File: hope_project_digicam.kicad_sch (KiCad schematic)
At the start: 22 parts, among them J1 TFT_Pin_Socket, J1 USB_C_Receptacle_USB2.0_16P, J2 SD_Card_Port, J3 Camera_Pin_Out, J4 Lipo battery input, Q1 NMOS, SW1 SW_Push, SW2 Reset, SW3 Boot, U1 ESP32-S3-WROOM-1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

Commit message: finished schematic
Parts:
- removed C1: 1uF, symbol Device:C
- removed U2: AP7332-3333W6-7, SOT26_DIO, symbol 2026-03-12_05-38-18:AP7332-3333W6-7
- added C5: 0.1uF, symbol Device:C
- added C6: 22uF, symbol Device:C
- added D2: D_Schottky, symbol Device:D_Schottky
- added Q2: PMOS, symbol Simulation_SPICE:PMOS
- added R10, R11, R7, R8, R9: 10k, symbol Device:R
- added R12: 100k, symbol Device:R
- added U3: AP2112K-3.3, Package_TO_SOT_SMD:SOT-23-5, symbol Regulator_Linear:AP2112K-3.3
- J4: value Lipo battery input -> Lipo batt in
- R5: value R -> 10
- R6: value R -> 10k
- renumbered J1 to J5
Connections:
- net +3.3V: now also J2.4 (VDD), J3.1 (Pin_1), J5.1 (Pin_1), R5.2, C5.1, C6.1, R10.1, R11.1, R7.1, R8.1, R9.1, U3.5 (VOUT); no longer C2.1
- net GND: now also J2.3 (VSS), J2.6 (VSS__1), J2.G1 (GND), J2.G2 (GND__1), J3.2 (Pin_2), J5.3 (Pin_3), SW1.2, C5.2, C6.2, R12.1, U3.2 (GND)
- net TFT_SDCS: now reaches J5.10 (Pin_10)
- net TFT_LIT: now reaches J5.11 (Pin_11)
- net TFT_LIT: now also U1.25 (IO48)
- net 3.3V_OUT: now reaches J5.2 (Pin_2)
- net TFT_SCK: now reaches J5.4 (Pin_4)
- net TFT_SCK: now also U1.31 (IO38)
- net TFT_MISO: now reaches J5.5 (Pin_5)
- net TFT_MOSI: now reaches J5.6 (Pin_6)
- net TFT_MOSI: now also U1.32 (IO39)
- net TFT_CS: now reaches J5.7 (Pin_7)
- net TFT_CS: now also U1.17 (IO9)
- net TFT_RST: now reaches J5.8 (Pin_8)
- net TFT_RST: now also C4.2, R1.2, SW2.2, U1.3 (EN)
- net TFT_DC: now reaches J5.9 (Pin_9)
- net TFT_DC: now also U1.16 (IO46)
- net SD_CS: now reaches J2.1 (DAT3/CD)
- net SD_CS: now also U1.18 (IO10), R9.2
- net SD_MOSI: now reaches J2.2 (CMD)
- net SD_MOSI: now also U1.19 (IO11), R7.2
- net SD_SCK: now reaches J2.5 (CLK)
- net SD_SCK: now also U1.20 (IO12)
- net SD_MISO: now reaches J2.7 (DAT0)
- net SD_MISO: now also U1.21 (IO13), R8.2
- net SD_DAT1: now reaches J2.8 (DAT1)
- net SD_DAT1: now also R10.2
- net SD_DAT2: now reaches J2.9 (DAT2)
- net SD_DAT2: now also R11.2
- net CAM_D8: now reaches J3.10 (Pin_10)
- net CAM_D8: now also U1.10 (IO17)
- net CAM_D7: now reaches J3.11 (Pin_11)
- net CAM_D7: now also U1.9 (IO16)
- net CAM_D6: now reaches J3.12 (Pin_12)
- net CAM_D6: now also U1.8 (IO15)
- net CAM_D5: now reaches J3.13 (Pin_13)
- net CAM_D5: now also U1.7 (IO7)
- net CAM_D4: now reaches J3.14 (Pin_14)
- net CAM_D4: now also U1.6 (IO6)
- net CAM_D3: now reaches J3.15 (Pin_15)
- net CAM_D3: now also U1.5 (IO5)
- net CAM_D2: now reaches J3.16 (Pin_16)
- net CAM_D2: now also U1.4 (IO4)
- net CAM_RT: now reaches J3.17 (Pin_17)
- net CAM_PD: now reaches J3.18 (Pin_18)
- net CAM_SCL: now reaches J3.3 (Pin_3)
- net CAM_SCL: now also U1.39 (IO1)
- net CAM_SDA: now reaches J3.4 (Pin_4)
- net CAM_SDA: now also U1.38 (IO2)
- net CAM_VS: now reaches J3.5 (Pin_5)
- net CAM_VS: now also U1.24 (IO47)
- net CAM_HS: now reaches J3.6 (Pin_6)
- net CAM_HS: now also U1.23 (IO21)
- net CAM_PC: now reaches J3.7 (Pin_7)
- net CAM_PC: now also U1.12 (IO8)
- net CAM_XC: now reaches J3.8 (Pin_8)
- net CAM_XC: now also U1.15 (IO3)
- net CAM_D9: now reaches J3.9 (Pin_9)
- net CAM_D9: now also U1.11 (IO18)
- net CAM_TRIGGER: now reaches SW1.1
- net CAM_TRIGGER: now also U1.22 (IO14)
- net LED: now reaches R4.1
- net LED: now also U1.26 (IO45)
- net VCC renamed VBUS
- net VBUS: now also D2.2 (A), Q2.2 (G), R12.2; no longer J4.2 (Pin_2), R5.2
- new net +BATT: J4.2 (Pin_2), Q2.1 (D)
- new net PWR_IN: C2.1, D2.1 (K), Q2.3 (S), U3.1 (VIN), U3.3 (EN)
- no-connect marks 2 -> 17
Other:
- note added: "Camera Button Trigger"
- note added: "Camera Pins"
- note added: "ESP32-S3-WROOM-1"
- note added: "Flash / LED"
- note added: "Lipo power in + LDO to 3.3V"
- note added: "SD Card Port"
- note added: "TFT Screen Pins"
- note added: "TFT_MISO is 3.3V because write-only, can leave unconnected"
- note added: "USB-C Power and Data"
- moved on the sheet: C3, C4, D1, J1, J2, J3, J4, J5, Q1, R1, R2, R3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

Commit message: added test points
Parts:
- added J6: extra, symbol Connector:Conn_01x02_Socket
- added TP1, TP10, TP11, TP12, TP13, TP2, TP3, TP4, TP5, TP6, TP7, TP8, TP9: TestPoint, symbol Connector:TestPoint
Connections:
- net +3.3V: now also TP1.1
- net +BATT: now also TP2.1
- net CAM_PC: now also TP9.1
- net CAM_SCL: now also TP7.1
- net CAM_SDA: now also TP8.1
- net GND: now also TP5.1, TP6.1
- net PWR_IN: now also TP3.1
- net SD_MISO: now also TP12.1
- net SD_MOSI: now also TP11.1
- net SD_SCK: now also TP10.1
- net VBUS: now also TP4.1
- net at Q1.2 (G), R4.2, R6.1: now also TP13.1
- net at U1.36 (RXD0): now also J6.2 (Pin_2)
- net at U1.37 (TXD0): now also J6.1 (Pin_1)
- no-connect marks 17 -> 15
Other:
- moved on the sheet: D1, J3, J5, Q1, R4, R5, R6, SW1

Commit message: layout progress
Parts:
- C2, C3, C4: footprint (none) -> HOPE DigiCam:1uF_Cap
- C5: footprint (none) -> HOPE DigiCam:0.1u_Cap
- C6: footprint (none) -> HOPE DigiCam:22u_Cap
- D1: footprint (none) -> LED_SMD:LED_1206_3216Metric
- D2: footprint (none) -> HOPE DigiCam:Shottky_Diode
- J1: footprint (none) -> HOPE DigiCam:USB_C_Receptacle
- J2: footprint 10067847-001RLF:AMPHENOL_10067847-001RLF -> HOPE DigiCam:SD_Card_Conn
- J3, J5, J6: footprint (none) -> HOPE DigiCam:40_Pin_Conn
- J4: footprint (none) -> HOPE DigiCam:Right_Angle_Conn
- Q1: footprint (none) -> HOPE DigiCam:NMOS
- Q2: footprint (none) -> HOPE DigiCam:PMOS
- R1, R5: footprint (none) -> HOPE DigiCam:10_Res
- R10, R11, R6, R7, R8, R9: footprint (none) -> HOPE DigiCam:10k_Res
- R12: footprint (none) -> HOPE DigiCam:100k_Res
- R2, R3: footprint (none) -> HOPE DigiCam:5.1k_Res
- R4: footprint (none) -> HOPE DigiCam:100_Res
- SW2, SW3: footprint (none) -> HOPE DigiCam:SW2_SW3
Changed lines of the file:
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@@
 			)
 		)
-		(property "Footprint" ""
+		(property "Footprint" "HOPE DigiCam:Right_Angle_Conn"
 			(at 26.67 34.29 0)
 			(effects
@@
 			)
 		)
-		(property "Footprint" ""
+		(property "Footprint" "HOPE DigiCam:40_Pin_Conn"
 			(at 234.95 100.33 0)
 			(effects
@@
 			)
 		)
-		(property "Footprint" ""
+		(property "Footprint" "HOPE DigiCam:5.1k_Res"
 			(at 62.738 80.01 90)
 			(effects
@@
 			)
 		)
-		(property "Footprint" "10067847-001RLF:AMPHENOL_10067847-001RLF"
+		(property "Footprint" "HOPE DigiCam:SD_Card_Conn"
 			(at 83.82 153.67 0)
 			(effects
@@
 			)
 		)
-		(property "Footprint" ""
+		(property "Footprint" "HOPE DigiCam:PMOS"
 			(at 80.01 27.94 0)
 			(effects
@@
 			)
 		)
-		(property "Footprint" ""
+		(property "Footprint" "HOPE DigiCam:10_Res"
 			(at 106.172 63.5 90)
 			(effects
@@
 			)
 		)
-		(property "Footprint" ""
+		(property "Footprint" "HOPE DigiCam:22u_Cap"
 			(at 187.6552 69.85 0)
 			(effects
@@
 			)
 		)
-		(property "Footprint" ""
+		(property "Footprint" "HOPE DigiCam:SW2_SW3"
 			(at 96.52 83.82 0)
 			(effects
@@
 			)
 		)
-		(property "Footprint" ""
+		(property "Footprint" "HOPE DigiCam:40_Pin_Conn"
 			(at 165.1 67.31 0)
 			(effects
@@
 			)
 		)
-		(property "Footprint" ""
+		(property "Footprint" "HOPE DigiCam:SW2_SW3"
 			(at 99.06 62.23 0)
 			(effects
@@
 			)
 		)
-		(property "Footprint" ""
+		(property "Footprint" "HOPE DigiCam:NMOS"
 			(at 163.83 172.72 0)
 			(effects
@@
 			)
 		)
-		(property "Footprint" ""
+		(property "Footprint" "HOPE DigiCam:1uF_Cap"
 			(at 103.8352 36.83 0)
 			(effects
@@
 			)
 		)
-		(property "Footprint" ""
+		(property "Footprint" "HOPE DigiCam:40_Pin_Conn"
 			(at 224.79 148.59 0)
 			(effects
@@
 			)
 		)
-		(property "Footprint" ""
+		(property "Footprint" "HOPE DigiCam:5.1k_Res"
 			(at 70.358 77.47 90)
 			(effects
@@
 			)
 		)
-		(property "Footprint" ""
+		(property "Footprint" "HOPE DigiCam:10k_Res"
 			(at 40.132 179.07 90)
 			(effects
@@
 			)
 		)
-		(property "Footprint" ""
+		(property "Footprint" "HOPE DigiCam:10k_Res"
 			(at 27.432 179.07 90)
 			(effects
@@
 			)
 		)
-		(property "Footprint" ""
+		(property "Footprint" "HOPE DigiCam:10k_Res"
 			(at 54.102 149.86 90)
 			(effects
@@
 			)
 		)
-		(property "Footprint" ""
+		(property "Footprint" "HOPE DigiCam:10_Res"
 			(at 163.068 154.94 90)
 			(effects
@@
 			)
 		)
-		(property "Footprint" ""
+		(property "Footprint" "HOPE DigiCam:100k_Res"
 			(at 67.818 34.29 90)
 			(effects
@@
 			)
 		)
-		(property "Footprint" ""
+		(property "Footprint" "HOPE DigiCam:0.1u_Cap"
 			(at 173.6852 69.85 0)
 			(effects
@@
 			)
 		)
-		(property "Footprint" ""
+		(property "Footprint" "LED_SMD:LED_1206_3216Metric"
 			(at 161.29 163.83 0)
 			(effects
@@
 			)
 		)
-		(property "Footprint" ""
+		(property "Footprint" "HOPE DigiCam:1uF_Cap"
 			(at 102.87 73.9648 0)
 			(effects
@@
 			)
 		)
-		(property "Footprint" ""
+		(property "Footprint" "HOPE DigiCam:10k_Res"
 			(at 24.892 160.02 90)
 			(effects
@@
 			)
 		)
-		(property "Footprint" ""
+		(property "Footprint" "HOPE DigiCam:10k_Res"
 			(at 37.592 152.4 90)
 			(effects
@@
 			)
 		)
-		(property "Footprint" ""
+		(property "Footprint" "HOPE DigiCam:100_Res"
 			(at 147.32 177.038 90)
 			(effects
@@
 			)
 		)
-		(property "Footprint" ""
+		(property "Footprint" "HOPE DigiCam:10k_Res"
 			(at 154.94 185.928 90)
 			(effects
@@
 			)
 		)
-		(property "Footprint" ""
+		(property "Footprint" "HOPE DigiCam:USB_C_Receptacle"
 			(at 39.37 83.82 0)
 			(effects
@@
 			)
 		)
-		(property "Footprint" ""
+		(property "Footprint" "HOPE DigiCam:Shottky_Diode"
 			(at 57.15 63.5 0)
 			(effects
@@
 			)
 		)
-		(property "Footprint" ""
+		(property "Footprint" "HOPE DigiCam:1uF_Cap"
 			(at 136.8552 36.83 0)
 			(effects

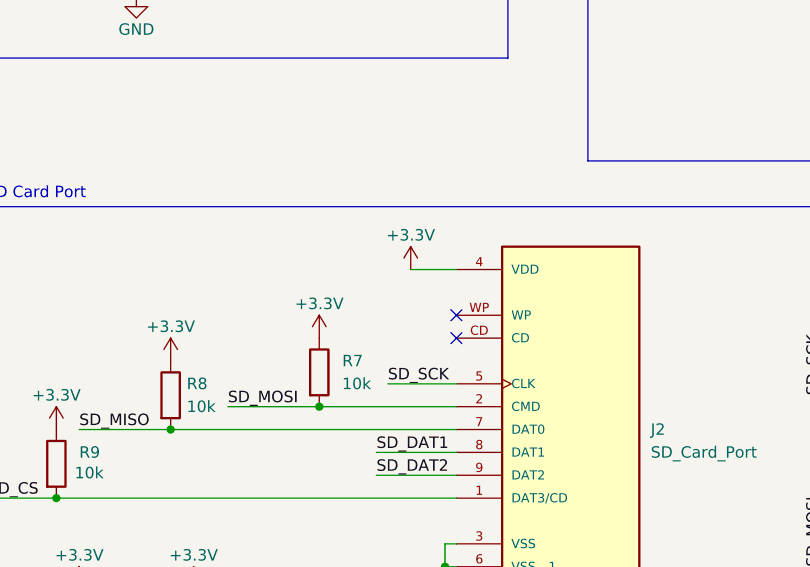
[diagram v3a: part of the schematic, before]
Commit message: fixed footprints
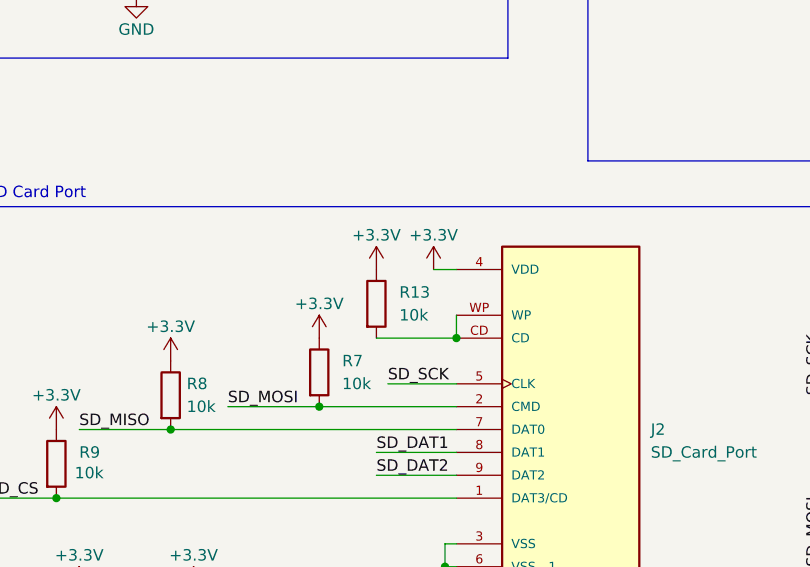
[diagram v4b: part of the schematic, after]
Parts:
- added R13: 10k, HOPE DigiCam:10k_Res, symbol Device:R
- J3: footprint HOPE DigiCam:40_Pin_Conn -> Connector_PinSocket_2.54mm:PinSocket_2x09_P2.54mm_Vertical
- J5: footprint HOPE DigiCam:40_Pin_Conn -> Connector_PinSocket_2.54mm:PinSocket_1x11_P2.54mm_Vertical
- SW1: footprint (none) -> HOPE DigiCam:SW2_SW3
- TP1, TP10, TP11, TP12, TP13, TP2, TP3, TP4, TP5, TP6, TP7, TP8, TP9: footprint (none) -> TestPoint:TestPoint_Plated_Hole_D2.0mm
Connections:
- net +3.3V: now also R13.1
- net at J2.CD: now also J2.WP, R13.2
- no-connect marks 15 -> 13
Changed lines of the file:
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@@
 	)
 	(junction
+		(at 71.12 146.05)
+		(diameter 0)
+		(color 0 0 0 0)
+	)
+	(junction
 		(at 39.37 156.21)
 		(diameter 0)
@@
 	)
 	(no_connect
-		(at 71.12 146.05)
-	)
-	(no_connect
-		(at 71.12 143.51)
-	)
-	(no_connect
 		(at 50.8 96.52)
 	)
@@
 	(wire
 		(pts
+			(xy 62.23 146.05) (xy 71.12 146.05)
+		)
+		(stroke
+			(width 0)
+			(type default)
+		)
+	)
+	(wire
+		(pts
 			(xy 219.71 105.41) (xy 229.87 105.41)
 		)
@@
 	(wire
 		(pts
+			(xy 68.58 138.43) (xy 71.12 138.43)
+		)
+		(stroke
+			(width 0)
+			(type default)
+		)
+	)
+	(wire
+		(pts
 			(xy 154.94 92.71) (xy 165.1 92.71)
 		)
@@
 	(wire
 		(pts
+			(xy 71.12 143.51) (xy 71.12 146.05)
+		)
+		(stroke
+			(width 0)
+			(type default)
+		)
+	)
+	(wire
+		(pts
 			(xy 209.55 153.67) (xy 219.71 153.67)
 		)
@@
 	(wire
 		(pts
-			(xy 66.04 138.43) (xy 71.12 138.43)
-		)
-		(stroke
-			(width 0)
-			(type default)
-		)
-	)
-	(wire
-		(pts
 			(xy 105.41 67.31) (xy 105.41 74.93)
 		)
@@
 			)
 		)
-		(property "Footprint" ""
+		(property "Footprint" "TestPoint:TestPoint_Plated_Hole_D2.0mm"
 			(at 116.84 180.34 0)
 			(effects
@@
 			)
 		)
-		(property "Footprint" "HOPE DigiCam:40_Pin_Conn"
+		(property "Footprint" "Connector_PinSocket_2.54mm:PinSocket_1x11_P2.54mm_Vertical"
 			(at 234.95 100.33 0)
 			(effects
@@
 			)
 		)
-		(property "Footprint" ""
+		(property "Footprint" "TestPoint:TestPoint_Plated_Hole_D2.0mm"
 			(at 163.83 35.56 0)
 			(effects
@@
 			)
 		)
-		(property "Footprint" ""
+		(property "Footprint" "TestPoint:TestPoint_Plated_Hole_D2.0mm"
 			(at 156.21 171.45 0)
 			(effects
@@
 			)
 		)
-		(property "Footprint" ""
+		(property "Footprint" "TestPoint:TestPoint_Plated_Hole_D2.0mm"
 			(at 116.84 142.24 0)
 			(effects
@@
 			)
 		)
-		(property "Footprint" ""
+		(property "Footprint" "TestPoint:TestPoint_Plated_Hole_D2.0mm"
 			(at 166.37 26.67 0)
 			(effects
@@
 			)
 		)
-		(property "Footprint" "HOPE DigiCam:40_Pin_Conn"
+		(property "Footprint" "Connector_PinSocket_2.54mm:PinSocket_2x09_P2.54mm_Vertical"
 			(at 224.79 148.59 0)
 			(effects
@@
 			)
 		)
-		(property "Footprint" ""
+		(property "Footprint" "TestPoint:TestPoint_Plated_Hole_D2.0mm"
 			(at 181.61 35.56 0)
 			(effects
@@
 			)
 		)
-		(property "Footprint" ""
+		(property "Footprint" "TestPoint:TestPoint_Plated_Hole_D2.0mm"
 			(at 274.32 144.78 0)
 			(effects
@@
 	(symbol
 		(lib_id "power:+3.3V")
-		(at 66.04 138.43 0)
+		(at 62.23 138.43 0)
+		(unit 1)
+		(exclude_from_sim no)
+		(in_bom yes)
+		(on_board yes)
+		(dnp no)
+		(property "Reference" "#PWR039"
+			(at 62.23 142.24 0)
+			(effects
+				(font
+					(size 1.27 1.27)
+				)
+				(hide yes)
+			)
+		)
+		(property "Value" "+3.3V"
+			(at 62.23 134.62 0)
+			(effects
+				(font
+					(size 1.27 1.27)
+				)
+			)
+		)
+		(property "Footprint" ""
+			(at 62.23 138.43 0)
+			(effects
+				(font
+					(size 1.27 1.27)
+				)
+				(hide yes)
+			)
+		)
+		(property "Datasheet" ""
+			(at 62.23 138.43 0)
+			(effects
+				(font
+					(size 1.27 1.27)
+				)
+				(hide yes)
+			)
+		)
+		(property "Description" "Power symbol creates a global label with name \"+3.3V\""
+			(at 62.23 138.43 0)
+			(effects
+				(font
+					(size 1.27 1.27)
+				)
+				(hide yes)
+			)
+		)
+		(pin "1"
+		)
+		(instances
+			(project "hope_project_digicam"
+				(path "/cbe9fd98-ee86-44ac-bda3-802b626f1144"
+					(reference "#PWR039")
+					(unit 1)
+				)
+			)
+		)
+	)
+	(symbol
+		(lib_id "power:+3.3V")
+		(at 68.58 138.43 0)
 		(unit 1)
 		(exclude_from_sim no)
@@
 		(dnp no)
 		(property "Reference" "#PWR024"
-			(at 66.04 142.24 0)
+			(at 68.58 142.24 0)
 			(effects
 				(font
@@
 		)
 		(property "Value" "+3.3V"
-			(at 66.04 134.62 0)
+			(at 68.58 134.62 0)
 			(effects
 				(font
@@
 		)
 		(property "Footprint" ""
-			(at 66.04 138.43 0)
+			(at 68.58 138.43 0)
 			(effects
 				(font
@@
 		)
 		(property "Datasheet" ""
-			(at 66.04 138.43 0)
+			(at 68.58 138.43 0)
 			(effects
 				(font
@@
 		)
 		(property "Description" "Power symbol creates a global label with name \"+3.3V\""
-			(at 66.04 138.43 0)
+			(at 68.58 138.43 0)
 			(effects
 				(font
@@
 			)
 		)
-		(property "Footprint" ""
+		(property "Footprint" "HOPE DigiCam:SW2_SW3"
 			(at 226.06 60.96 0)
 			(effects
@@
 			)
 		)
-		(property "Footprint" ""
+		(property "Footprint" "TestPoint:TestPoint_Plated_Hole_D2.0mm"
 			(at 116.84 161.29 0)
 			(effects
@@
 			)
 		)
-		(property "Footprint" ""
+		(property "Footprint" "TestPoint:TestPoint_Plated_Hole_D2.0mm"
 			(at 257.81 135.89 0)
 			(effects
@@
 			)
 		)
-		(property "Footprint" ""
+		(property "Footprint" "TestPoint:TestPoint_Plated_Hole_D2.0mm"
 			(at 257.81 153.67 0)
 			(effects
@@
 	)
 	(symbol
+		(lib_id "Device:R")
+		(at 62.23 142.24 0)
+		(unit 1)
+		(exclude_from_sim no)
+		(in_bom yes)
+		(on_board yes)
+		(dnp no)
+		(property "Reference" "R13"
+			(at 64.77 140.9699 0)
+			(effects
+				(font
+					(size 1.27 1.27)
+				)
+				(justify left)
+			)
+		)
+		(property "Value" "10k"
+			(at 64.77 143.5099 0)
+			(effects
+				(font
+					(size 1.27 1.27)
+				)
+				(justify left)
+			)
+		)
+		(property "Footprint" "HOPE DigiCam:10k_Res"
+			(at 60.452 142.24 90)
+			(effects
+				(font
+					(size 1.27 1.27)
+				)
+				(hide yes)
+			)
+		)
+		(property "Datasheet" "~"
+			(at 62.23 142.24 0)
+			(effects
+				(font
+					(size 1.27 1.27)
+				)
+				(hide yes)
+			)
+		)
+		(property "Description" "Resistor"
+			(at 62.23 142.24 0)
+			(effects
+				(font
+					(size 1.27 1.27)
+				)
+				(hide yes)
+			)
+		)
+		(pin "1"
+		)
+		(pin "2"
+		)
+		(instances
+			(project "hope_project_digicam"
+				(path "/cbe9fd98-ee86-44ac-bda3-802b626f1144"
+					(reference "R13")
+					(unit 1)
+				)
+			)
+		)
+	)
+	(symbol
 		(lib_id "power:+3.3V")
 		(at 161.29 148.59 0)
@@
 			)
 		)
-		(property "Footprint" ""
+		(property "Footprint" "TestPoint:TestPoint_Plated_Hole_D2.0mm"
 			(at 193.04 26.67 0)
 			(effects
@@
 			)
 		)
-		(property "Footprint" ""
+		(property "Footprint" "TestPoint:TestPoint_Plated_Hole_D2.0mm"
 			(at 200.66 35.56 0)
 			(effects
@@
 			)
 		)
-		(property "Footprint" ""
+		(property "Footprint" "TestPoint:TestPoint_Plated_Hole_D2.0mm"
 			(at 217.17 35.56 0)
 			(effects

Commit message: Add files via upload
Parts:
- J3: footprint Connector_PinSocket_2.54mm:PinSocket_2x09_P2.54mm_Vertical -> HOPE DigiCam:Cam Module
- J5: footprint Connector_PinSocket_2.54mm:PinSocket_1x11_P2.54mm_Vertical -> HOPE DigiCam:TFT Module
- J6: footprint HOPE DigiCam:40_Pin_Conn -> Connector_PinSocket_2.54mm:PinSocket_1x02_P2.54mm_Vertical
- SW1: value SW_Push -> Cam Trigger
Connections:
- net CC2: now reaches J1.B5 (CC2), R3.2
- net CC1: now reaches J1.A5 (CC1), R2.2
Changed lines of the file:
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@@
 		)
 	)
+	(label "CC1"
+		(at 63.5 73.66 0)
+		(effects
+			(font
+				(size 1.27 1.27)
+			)
+			(justify left bottom)
+		)
+	)
 	(label "PWR_IN"
 		(at 77.47 43.18 90)
@@
 		)
 	)
+	(label "CC2"
+		(at 53.34 76.2 0)
+		(effects
+			(font
+				(size 1.27 1.27)
+			)
+			(justify left bottom)
+		)
+	)
 	(symbol
 		(lib_id "power:GND")
@@
 		)
 		(instances
-			(project ""
+			(project "hope_project_digicam"
 				(path "/cbe9fd98-ee86-44ac-bda3-802b626f1144"
 					(reference "J4")
@@
 			)
 		)
-		(property "Footprint" "Connector_PinSocket_2.54mm:PinSocket_1x11_P2.54mm_Vertical"
+		(property "Footprint" "HOPE DigiCam:TFT Module"
 			(at 234.95 100.33 0)
 			(effects
@@
 		)
 		(instances
-			(project ""
+			(project "hope_project_digicam"
 				(path "/cbe9fd98-ee86-44ac-bda3-802b626f1144"
 					(reference "J5")
@@
 		)
 		(instances
-			(project ""
+			(project "hope_project_digicam"
 				(path "/cbe9fd98-ee86-44ac-bda3-802b626f1144"
 					(reference "J2")
@@
 		)
 		(instances
-			(project ""
+			(project "hope_project_digicam"
 				(path "/cbe9fd98-ee86-44ac-bda3-802b626f1144"
 					(reference "Q2")
@@
 		)
 		(instances
-			(project ""
+			(project "hope_project_digicam"
 				(path "/cbe9fd98-ee86-44ac-bda3-802b626f1144"
 					(reference "R1")
@@
 		)
 		(instances
-			(project ""
+			(project "hope_project_digicam"
 				(path "/cbe9fd98-ee86-44ac-bda3-802b626f1144"
 					(reference "TP1")
@@
 			)
 		)
-		(property "Footprint" "HOPE DigiCam:40_Pin_Conn"
+		(property "Footprint" "Connector_PinSocket_2.54mm:PinSocket_1x02_P2.54mm_Vertical"
 			(at 165.1 67.31 0)
 			(effects
@@
 		)
 		(instances
-			(project ""
+			(project "hope_project_digicam"
 				(path "/cbe9fd98-ee86-44ac-bda3-802b626f1144"
 					(reference "Q1")
@@
 			)
 		)
-		(property "Footprint" "Connector_PinSocket_2.54mm:PinSocket_2x09_P2.54mm_Vertical"
+		(property "Footprint" "HOPE DigiCam:Cam Module"
 			(at 224.79 148.59 0)
 			(effects
@@
 		)
 		(instances
-			(project ""
+			(project "hope_project_digicam"
 				(path "/cbe9fd98-ee86-44ac-bda3-802b626f1144"
 					(reference "J3")
@@
 		)
 		(instances
-			(project ""
+			(project "hope_project_digicam"
 				(path "/cbe9fd98-ee86-44ac-bda3-802b626f1144"
 					(reference "R2")
@@
 		)
 		(instances
-			(project ""
+			(project "hope_project_digicam"
 				(path "/cbe9fd98-ee86-44ac-bda3-802b626f1144"
 					(reference "#PWR02")
@@
 			)
 		)
-		(property "Value" "SW_Push"
+		(property "Value" "Cam Trigger"
 			(at 226.06 60.96 0)
 			(effects
@@
 		)
 		(instances
-			(project ""
+			(project "hope_project_digicam"
 				(path "/cbe9fd98-ee86-44ac-bda3-802b626f1144"
 					(reference "SW1")
@@
 		)
 		(instances
-			(project ""
+			(project "hope_project_digicam"
 				(path "/cbe9fd98-ee86-44ac-bda3-802b626f1144"
 					(reference "R12")
@@
 		)
 		(instances
-			(project ""
+			(project "hope_project_digicam"
 				(path "/cbe9fd98-ee86-44ac-bda3-802b626f1144"
 					(reference "D1")
@@
 		)
 		(instances
-			(project ""
+			(project "hope_project_digicam"
 				(path "/cbe9fd98-ee86-44ac-bda3-802b626f1144"
 					(reference "C4")
@@
 		)
 		(instances
-			(project ""
+			(project "hope_project_digicam"
 				(path "/cbe9fd98-ee86-44ac-bda3-802b626f1144"
 					(reference "U3")
@@
 		)
 		(instances
-			(project ""
+			(project "hope_project_digicam"
 				(path "/cbe9fd98-ee86-44ac-bda3-802b626f1144"
 					(reference "#FLG01")
@@
 		)
 		(instances
-			(project ""
+			(project "hope_project_digicam"
 				(path "/cbe9fd98-ee86-44ac-bda3-802b626f1144"
 					(reference "R4")
@@
 		)
 		(instances
-			(project ""
+			(project "hope_project_digicam"
 				(path "/cbe9fd98-ee86-44ac-bda3-802b626f1144"
 					(reference "#PWR01")
@@
 		)
 		(instances
-			(project ""
+			(project "hope_project_digicam"
 				(path "/cbe9fd98-ee86-44ac-bda3-802b626f1144"
 					(reference "J1")
@@
 		)
 		(instances
-			(project ""
+			(project "hope_project_digicam"
 				(path "/cbe9fd98-ee86-44ac-bda3-802b626f1144"
 					(reference "D2")
@@
 		)
 		(instances
-			(project ""
+			(project "hope_project_digicam"
 				(path "/cbe9fd98-ee86-44ac-bda3-802b626f1144"
 					(reference "U1")
